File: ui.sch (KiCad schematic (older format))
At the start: 45 parts, among them SW1 SW_Push, SW2 SW_Push, SW3 SW_Push, SW4 SW_Push, SW5 SW_Push, SW8 JS202011SCQN, SW9 JS202011SCQN, U1 ICE40HX4K-TQ144

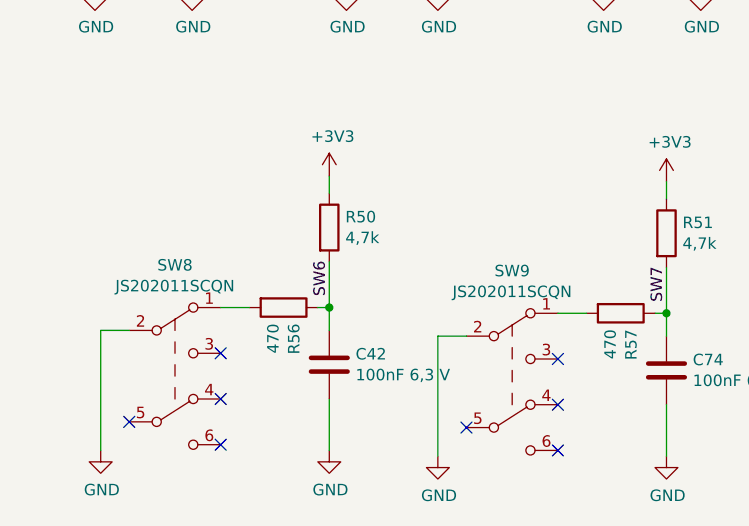
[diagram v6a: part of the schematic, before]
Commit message: Corrected a few footprints
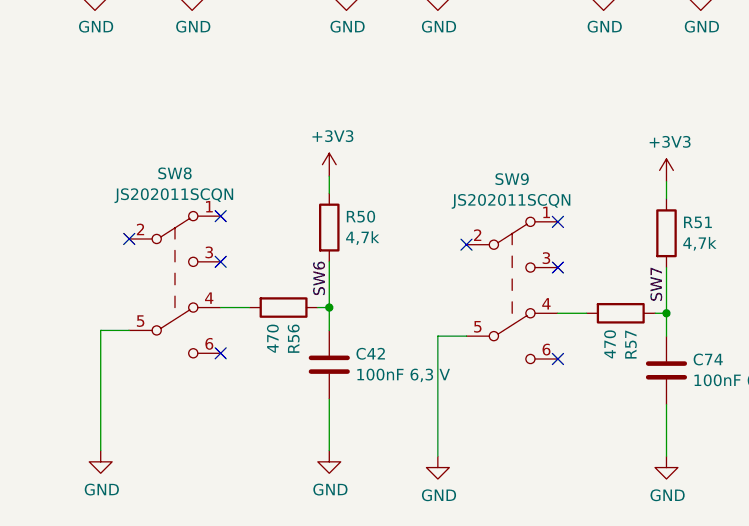
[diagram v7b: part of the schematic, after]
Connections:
- net GND: now also SW8.5 (B), SW9.5 (B); no longer SW8.2 (B), SW9.2 (B)
- net at SW8.1 (A): no longer R56.2
- net at SW8.4 (A): now also R56.2
- net at SW9.1 (A): no longer R57.2
- net at SW9.4 (A): now also R57.2
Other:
- moved on the sheet: SW8, SW9
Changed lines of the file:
@@
 L sw_dpdt:SW_DPDT SW?
 U 1 1 5E39AE94
-P 1275 5425
+P 1275 5025
 AR Path="/5CA8FBC7/5E39AE94" Ref="SW?"  Part="1"
 AR Path="/5CAB7CD4/5E39AE94" Ref="SW8"  Part="1"
-F 0 "SW8" H 1275 5910 50  0000 C CNN
-F 1 "JS202011SCQN" H 1275 5819 50  0000 C CNN
-F 2 "footprints:SW_SLIDE_DPDT_Slide_CK_JS202011SCQN_W3mm_P2.5mm_footprint" H 1275 5625 50  0001 C CNN
-F 3 "https://www.ckswitches.com/media/1422/js.pdf" H 1275 5625 50  0001 C CNN
-F 4 "C&K" H 1275 5425 50  0001 C CNN "Mfg Name"
-F 5 "JS202011SCQN" H 1275 5425 50  0001 C CNN "Mfg Part Num"
-F 6 "401-2002-1-ND" H 1275 5425 50  0001 C CNN "Digikey"
-F 7 "SWITCH SLIDE DPDT 300MA 6V" H 1275 5425 50  0001 C CNN "Description"
-F 8 "Spec" H 0   0   50  0001 C CNN "Spec"
-	1    1275 5425
+F 0 "SW8" H 1275 5510 50  0000 C CNN
+F 1 "JS202011SCQN" H 1275 5419 50  0000 C CNN
+F 2 "footprints:SW_SLIDE_DPDT_Slide_CK_JS202011SCQN_W3mm_P2.5mm_footprint" H 1275 5225 50  0001 C CNN
+F 3 "https://www.ckswitches.com/media/1422/js.pdf" H 1275 5225 50  0001 C CNN
+F 4 "C&K" H 1275 5025 50  0001 C CNN "Mfg Name"
+F 5 "JS202011SCQN" H 1275 5025 50  0001 C CNN "Mfg Part Num"
+F 6 "401-2002-1-ND" H 1275 5025 50  0001 C CNN "Digikey"
+F 7 "SWITCH SLIDE DPDT 300MA 6V" H 1275 5025 50  0001 C CNN "Description"
+F 8 "Spec" H 0   -400 50  0001 C CNN "Spec"
+	1    1275 5025
 	1    0    0    -1
 $EndComp
@@
 L sw_dpdt:SW_DPDT SW?
 U 1 1 5E3BC903
-P 2750 5450
+P 2750 5050
 AR Path="/5CA8FBC7/5E3BC903" Ref="SW?"  Part="1"
 AR Path="/5CAB7CD4/5E3BC903" Ref="SW9"  Part="1"
-F 0 "SW9" H 2750 5935 50  0000 C CNN
-F 1 "JS202011SCQN" H 2750 5844 50  0000 C CNN
-F 2 "footprints:SW_SLIDE_DPDT_Slide_CK_JS202011SCQN_W3mm_P2.5mm_footprint" H 2750 5650 50  0001 C CNN
-F 3 "https://www.ckswitches.com/media/1422/js.pdf" H 2750 5650 50  0001 C CNN
-F 4 "C&K" H 2750 5450 50  0001 C CNN "Mfg Name"
-F 5 "JS202011SCQN" H 2750 5450 50  0001 C CNN "Mfg Part Num"
-F 6 "401-2002-1-ND" H 2750 5450 50  0001 C CNN "Digikey"
-F 7 "SWITCH SLIDE DPDT 300MA 6V" H 2750 5450 50  0001 C CNN "Description"
-F 8 "Spec" H 0   0   50  0001 C CNN "Spec"
-	1    2750 5450
+F 0 "SW9" H 2750 5535 50  0000 C CNN
+F 1 "JS202011SCQN" H 2750 5444 50  0000 C CNN
+F 2 "footprints:SW_SLIDE_DPDT_Slide_CK_JS202011SCQN_W3mm_P2.5mm_footprint" H 2750 5250 50  0001 C CNN
+F 3 "https://www.ckswitches.com/media/1422/js.pdf" H 2750 5250 50  0001 C CNN
+F 4 "C&K" H 2750 5050 50  0001 C CNN "Mfg Name"
+F 5 "JS202011SCQN" H 2750 5050 50  0001 C CNN "Mfg Part Num"
+F 6 "401-2002-1-ND" H 2750 5050 50  0001 C CNN "Digikey"
+F 7 "SWITCH SLIDE DPDT 300MA 6V" H 2750 5050 50  0001 C CNN "Description"
+F 8 "Spec" H 0   -400 50  0001 C CNN "Spec"
+	1    2750 5050
 	1    0    0    -1
 $EndComp
@@
 $EndComp
 Wire Wire Line
-	2550 5250 2425 5250
-Wire Wire Line
 	3075 5150 2950 5150
-Wire Wire Line
-	2425 5250 2425 5775
 NoConn ~ 2950 5350
-NoConn ~ 2550 5650
-NoConn ~ 2950 5550
-NoConn ~ 2950 5750
-NoConn ~ 1075 5625
-NoConn ~ 1475 5725
-NoConn ~ 1475 5525
 NoConn ~ 1475 5325
 Wire Wire Line
@@
 Wire Wire Line
 	7975 2550 8250 2550
+Wire Wire Line
+	2550 5250 2425 5250
+Wire Wire Line
+	2425 5250 2425 5775
+NoConn ~ 2550 4850
+NoConn ~ 2950 4950
+NoConn ~ 2950 4750
+NoConn ~ 1075 4825
+NoConn ~ 1475 4925
+NoConn ~ 1475 4725
 $EndSCHEMATC

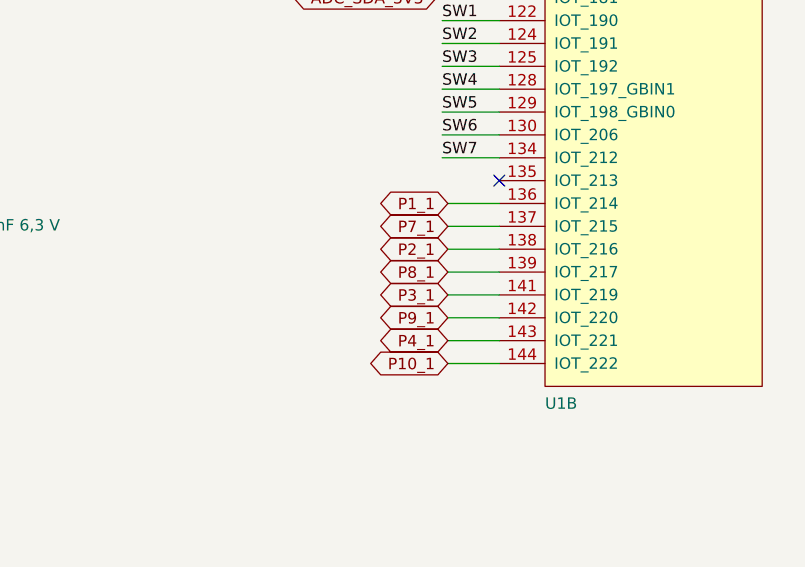
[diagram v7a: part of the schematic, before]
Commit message: Fixed rotated PMODs
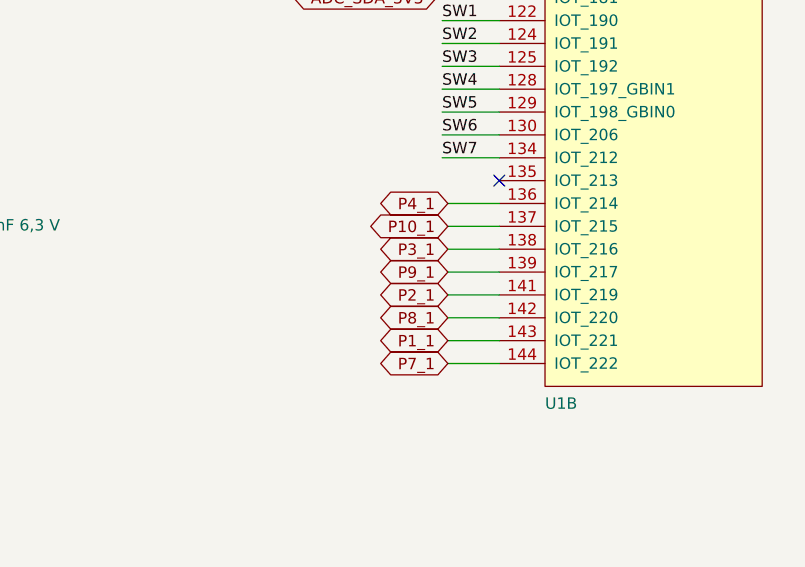
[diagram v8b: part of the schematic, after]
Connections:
- net P10_1: now also U1.137 (IOT_215); no longer U1.144 (IOT_222)
- net P1_1: now also U1.143 (IOT_221); no longer U1.136 (IOT_214)
- net P2_1: now also U1.141 (IOT_219); no longer U1.138 (IOT_216)
- net P3_1: now also U1.138 (IOT_216); no longer U1.141 (IOT_219)
- net P4_1: now also U1.136 (IOT_214); no longer U1.143 (IOT_221)
- net P7_1: now also U1.144 (IOT_222); no longer U1.137 (IOT_215)
- net P8_1: now also U1.142 (IOT_220); no longer U1.139 (IOT_217)
- net P9_1: now also U1.139 (IOT_217); no longer U1.142 (IOT_220)
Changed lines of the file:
@@
 NoConn ~ 8250 3350
 Wire Wire Line
-	8025 3450 8250 3450
+	8025 4150 8250 4150
+Wire Wire Line
+	8025 3950 8250 3950
+Wire Wire Line
+	8025 3750 8250 3750
+Wire Wire Line
+	8025 3550 8250 3550
+Wire Wire Line
+	8025 4050 8250 4050
+Wire Wire Line
+	8025 3850 8250 3850
 Wire Wire Line
 	8025 3650 8250 3650
 Wire Wire Line
-	8025 3850 8250 3850
-Wire Wire Line
-	8025 4050 8250 4050
-Wire Wire Line
-	8025 3550 8250 3550
-Wire Wire Line
-	8025 3750 8250 3750
-Wire Wire Line
-	8025 3950 8250 3950
-Wire Wire Line
-	8025 4150 8250 4150
+	8025 3450 8250 3450
+Text GLabel 8025 4050 0    50   BiDi ~ 0
+P1_1
+Text GLabel 8025 3850 0    50   BiDi ~ 0
+P2_1
+Text GLabel 8025 3650 0    50   BiDi ~ 0
+P3_1
 Text GLabel 8025 3450 0    50   BiDi ~ 0
-P1_1
-Text GLabel 8025 3650 0    50   BiDi ~ 0
-P2_1
-Text GLabel 8025 3850 0    50   BiDi ~ 0
-P3_1
-Text GLabel 8025 4050 0    50   BiDi ~ 0
 P4_1
+Text GLabel 8025 4150 0    50   BiDi ~ 0
+P7_1
+Text GLabel 8025 3950 0    50   BiDi ~ 0
+P8_1
+Text GLabel 8025 3750 0    50   BiDi ~ 0
+P9_1
 Text GLabel 8025 3550 0    50   BiDi ~ 0
-P7_1
-Text GLabel 8025 3750 0    50   BiDi ~ 0
-P8_1
-Text GLabel 8025 3950 0    50   BiDi ~ 0
-P9_1
-Text GLabel 8025 4150 0    50   BiDi ~ 0
 P10_1
 Text GLabel 7975 2550 0    50   BiDi ~ 0
